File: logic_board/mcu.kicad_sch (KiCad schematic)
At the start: 24 parts, among them J2 SOICBite, SW1 SW_Push, SW2 SW_Push, SW3 SW_Push, SW4 SW_Push, U1 STM32H7B0RBTx, Y1 Crystal_GND24

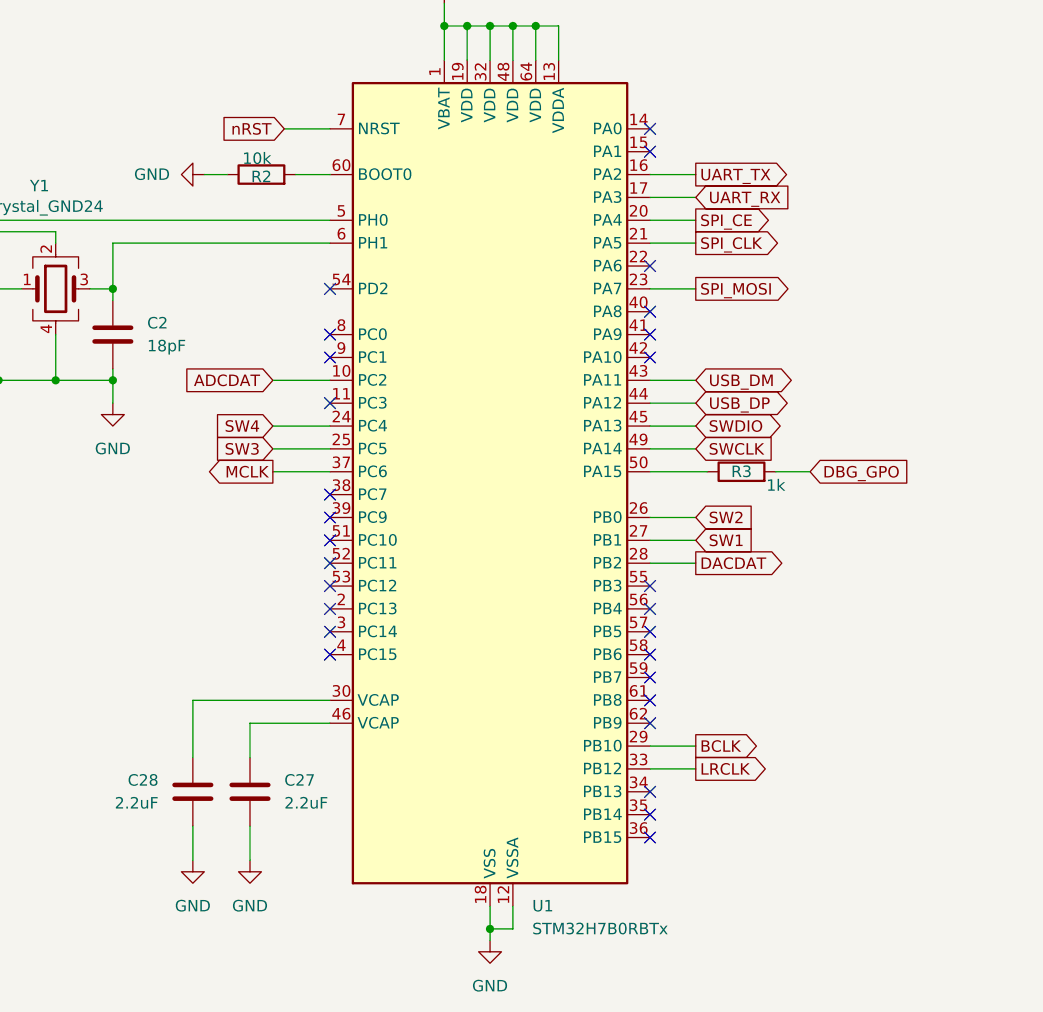
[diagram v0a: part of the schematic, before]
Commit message: Reoriented MCU and moved functions to different pins to try to get them closer to the chips they will connect to to minimize snaking and vias. Laid out bypass caps on codec.
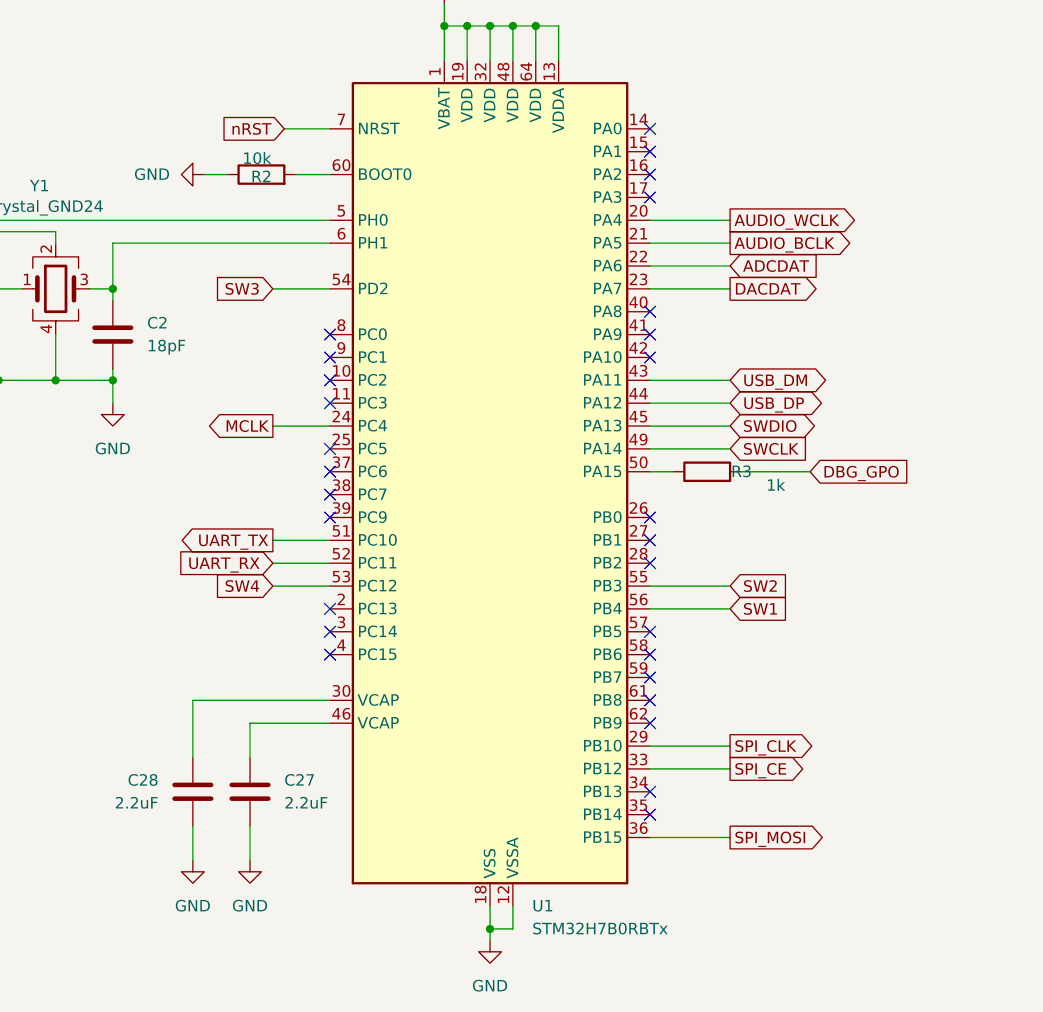
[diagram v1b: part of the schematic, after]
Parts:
- C17, C18, C19, C20, C21, C22: footprint Capacitor_SMD:C_0603_1608Metric -> Capacitor_SMD:C_0402_1005Metric
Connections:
- net BCLK is gone; now on net SPI_CLK: U1.29 (PB10)
- net LRCLK is gone; now on net SPI_CE: U1.33 (PB12)
- net ADCDAT: now also U1.22 (PA6); no longer U1.10 (PC2)
- net DACDAT: now also U1.23 (PA7); no longer U1.28 (PB2)
- net MCLK: now also U1.24 (PC4); no longer U1.37 (PC6)
- net SPI_CE: no longer U1.20 (PA4)
- net SPI_CLK: no longer U1.21 (PA5)
- net SPI_MOSI: now also U1.36 (PB15); no longer U1.23 (PA7)
- net SW1: now also U1.56 (PB4); no longer U1.27 (PB1)
- net SW2: now also U1.55 (PB3); no longer U1.26 (PB0)
- net SW3: now also U1.54 (PD2); no longer U1.25 (PC5)
- net SW4: now also U1.53 (PC12); no longer U1.24 (PC4)
- net UART_RX: now also U1.52 (PC11); no longer U1.17 (PA3)
- net UART_TX: now also U1.51 (PC10); no longer U1.16 (PA2)
- new net AUDIO_BCLK: U1.21 (PA5)
- new net AUDIO_WCLK: U1.20 (PA4)
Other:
- moved on the sheet: R3

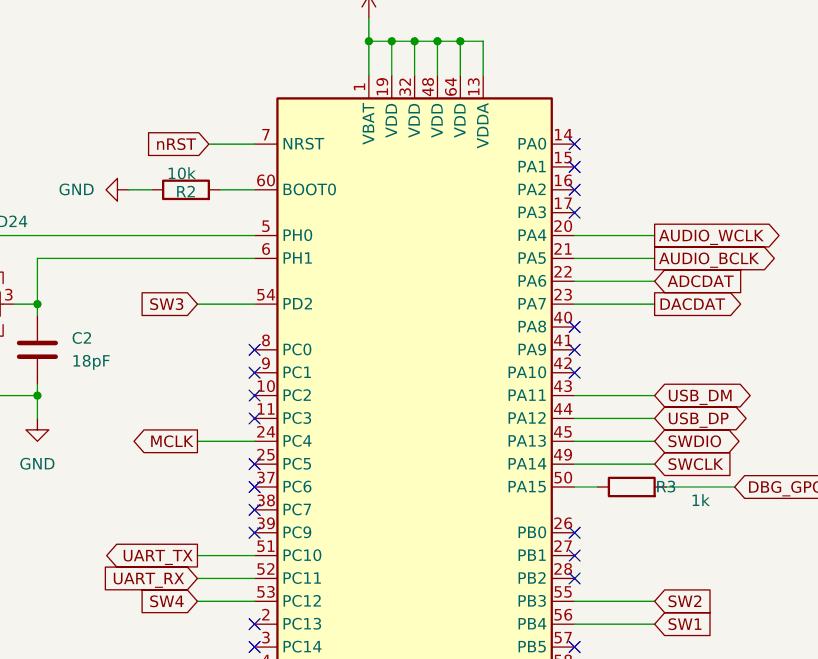
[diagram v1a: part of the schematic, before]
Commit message: Change charger to BQ25185
This one has power steering so it can run the MCU and charge simultaneously without charge termination problems.
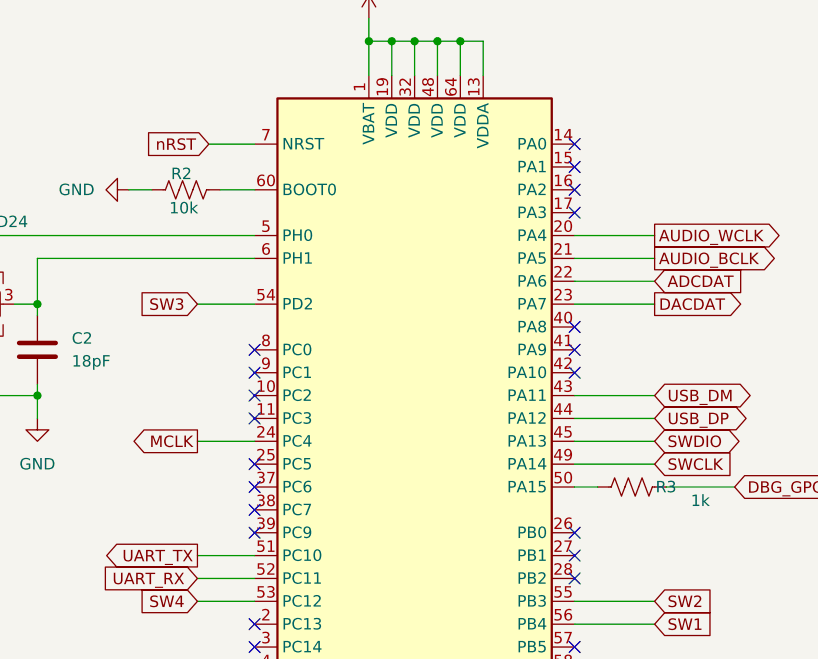
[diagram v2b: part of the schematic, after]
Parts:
- R2, R3: symbol Device:R -> Device:R_US
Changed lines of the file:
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@@
 	)
 	(symbol
-		(lib_id "Device:R")
+		(lib_id "Device:R_US")
 		(at 152.4 74.93 90)
 		(unit 1)
@@
 	)
 	(symbol
-		(lib_id "Device:R")
+		(lib_id "Device:R_US")
 		(at 102.87 41.91 90)
 		(unit 1)
@@
 		(dnp no)
 		(property "Reference" "R2"
-			(at 102.87 42.164 90)
+			(at 102.362 40.132 90)
 			(effects
 				(font
@@
 		)
 		(property "Value" "10k"
-			(at 102.362 40.132 90)
-			(effects
-				(font
+			(at 102.616 43.942 90)
+			(effects
+				(font

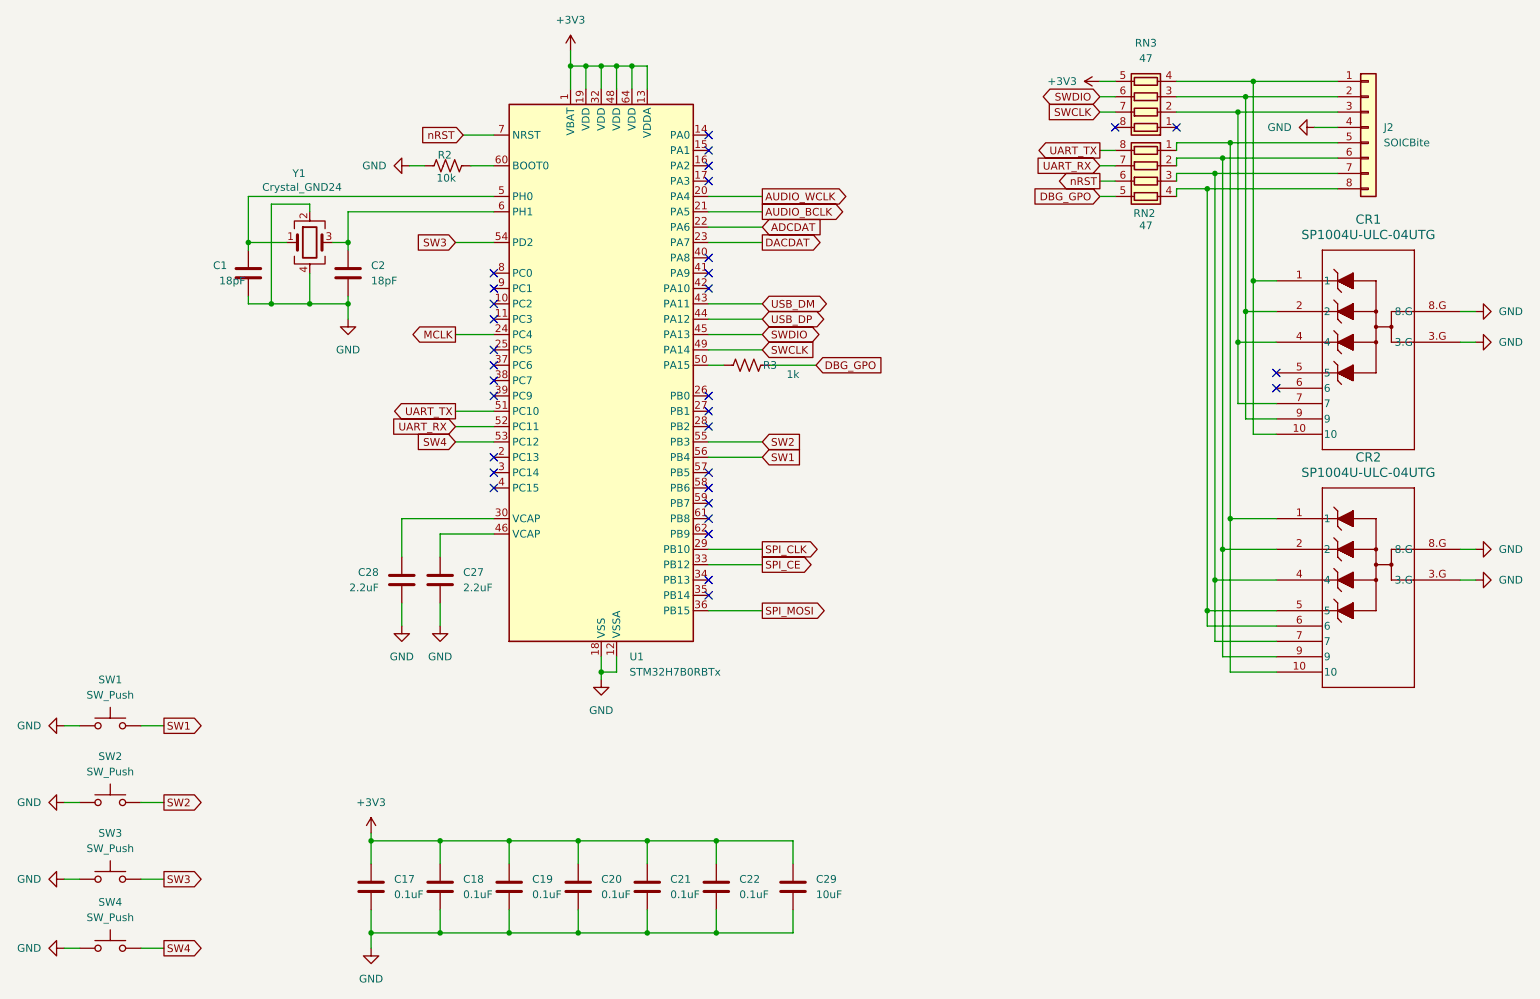
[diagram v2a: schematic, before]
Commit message: Change how charge management is handled
The LDO (and microcontroller) are now enabled even if the power switch is off when the device is charging.
Added a bi-color LED to indicate charging status (driven by microcontroller)
Charge status now routed to the microcontroller, as well as power switch status.

(Note this would also allow data transfer to the microcontroller when plugged in when the power switch is off, which is probably desirable).
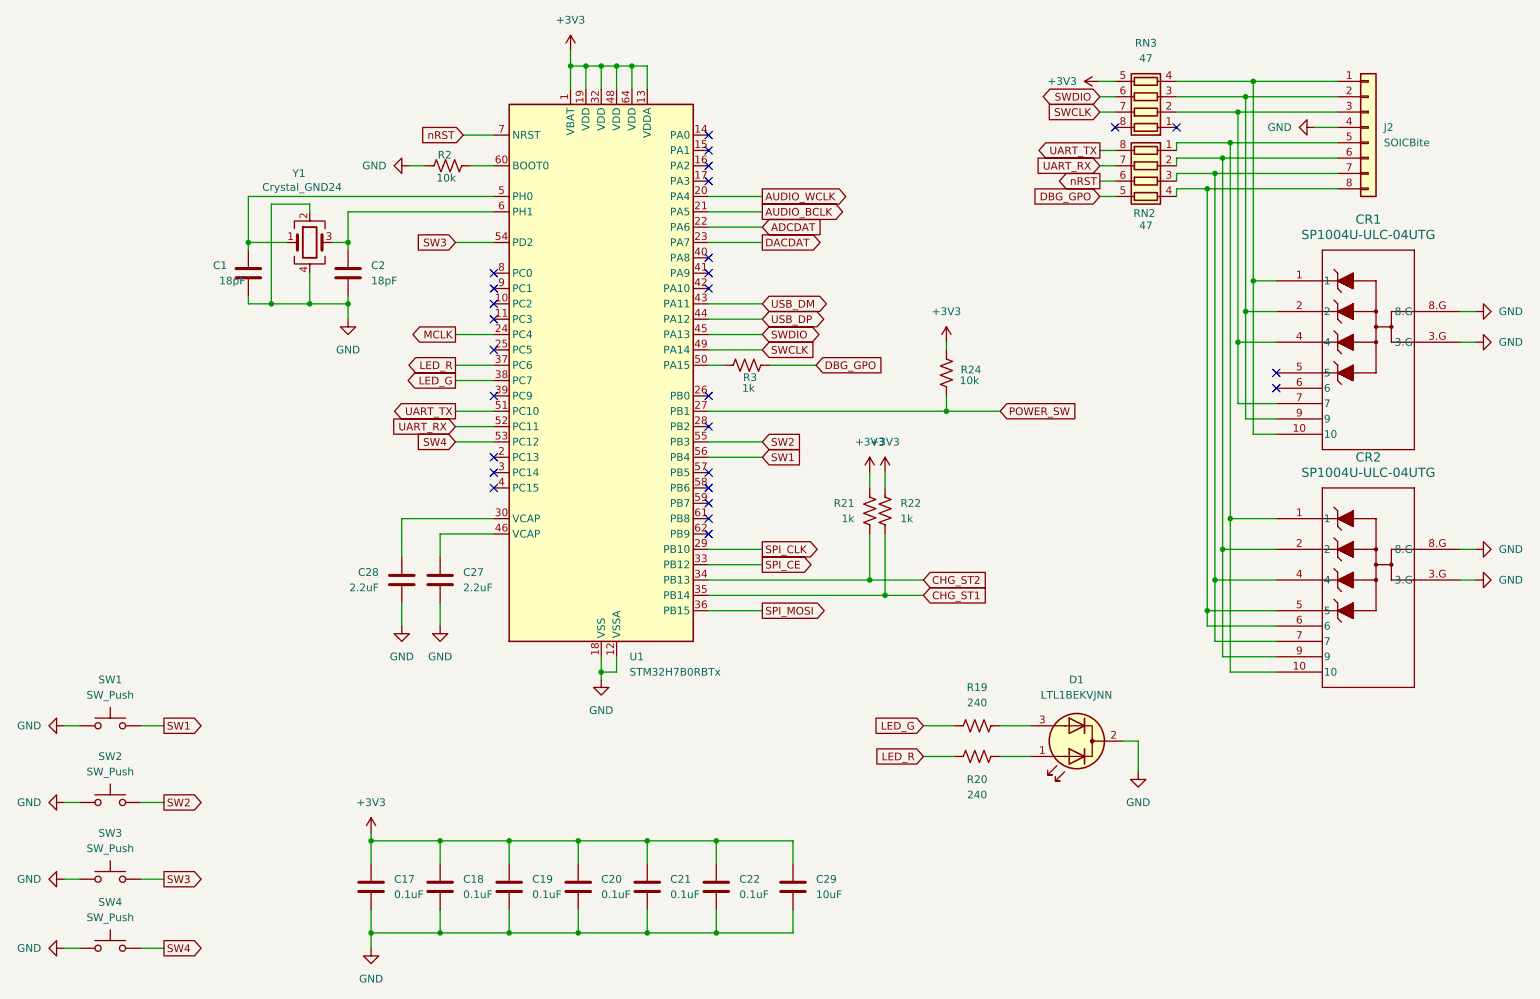
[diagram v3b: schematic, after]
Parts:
- added D1: LTL1BEKVJNN, LED_THT:LED_D5.0mm-3, symbol Device:LED_Dual_AKA
- added R19, R20: 240, Resistor_SMD:R_0603_1608Metric, symbol Device:R_US
- added R21, R22: 1k, Resistor_SMD:R_0603_1608Metric, symbol Device:R_US
- added R24: 10k, Resistor_SMD:R_0603_1608Metric, symbol Device:R_US
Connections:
- net +3V3: now also R21.1, R22.1, R24.2
- net GND: now also D1.2 (K)
- net POWER_SW: now reaches U1.27 (PB1)
- net POWER_SW: now also R24.1
- net CHG_ST2: now reaches U1.34 (PB13)
- net CHG_ST2: now also R21.2
- net CHG_ST1: now reaches U1.35 (PB14)
- net CHG_ST1: now also R22.2
- net LED_R: now reaches U1.37 (PC6)
- net LED_R: now also R20.1
- net LED_G: now reaches U1.38 (PC7)
- net LED_G: now also R19.1
- new net: D1.1 (A1), R20.2
- new net: D1.3 (A2), R19.2
- no-connect marks 32 -> 27

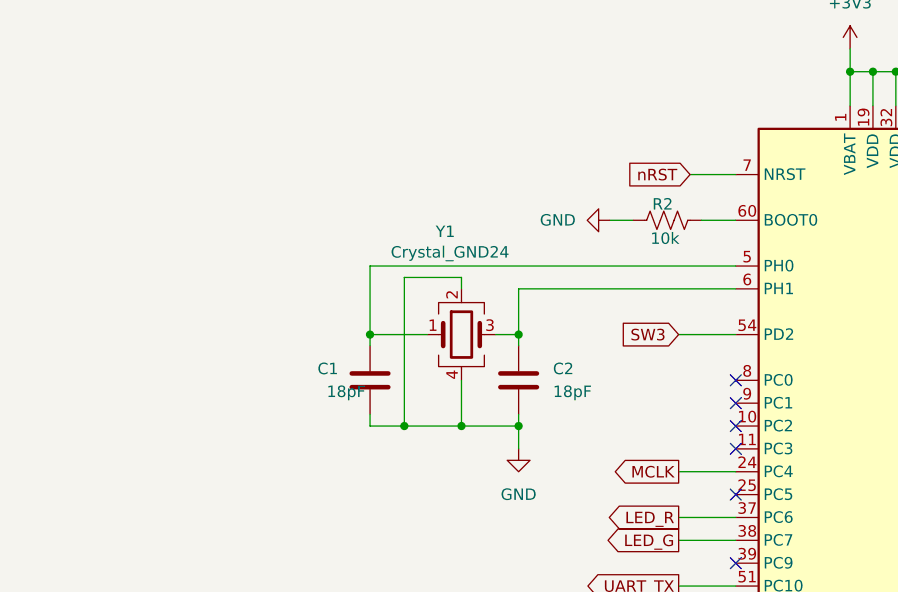
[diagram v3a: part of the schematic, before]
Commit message: Replace crystal with a more common variant, 8Mhz
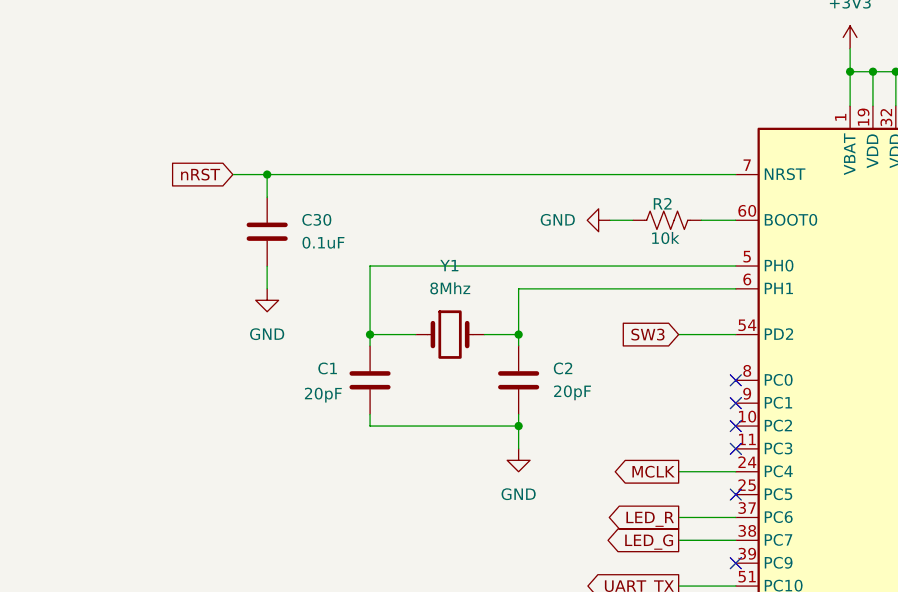
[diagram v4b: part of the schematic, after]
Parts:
- removed Y1: Crystal_GND24, Crystal:Crystal_SMD_3225-4Pin_3.2x2.5mm, symbol Device:Crystal_GND24
- added C30: 0.1uF, symbol Device:C
- added Y1: 8Mhz, Crystal:Crystal_SMD_5032-2Pin_5.0x3.2mm, symbol Device:Crystal
- C1, C2: value 18pF -> 20pF
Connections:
- net GND: now also C30.2
- net nRST: now also C30.1
- net at C1.1, U1.5 (PH0): now also Y1.1
- net at C2.1, U1.6 (PH1): now also Y1.2

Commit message: More component placement tweaking, mostly around audio section.
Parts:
- C30: footprint (none) -> Capacitor_SMD:C_0402_1005Metric
